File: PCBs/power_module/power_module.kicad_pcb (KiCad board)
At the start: 2 copper layers, 46.2 x 38.5 mm, 30 parts, among them J1 Conn_02x07_Odd_Even, J2 Conn_02x08_Odd_Even, J3 Conn_02x08_Odd_Even, J4 SM07B-GHS-TB, J5 SM03B-GHS-TB, J8 mlx_2pin, J9 SM08B-GHS-TB, U1 SN74LVC1T45DBV

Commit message: 3rd revision: corrected mounting holes
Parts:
- added H1: MountingHole, MountingHole:MountingHole_3.2mm_M3, F.Cu at (125.2, 45.2)
- added H2: MountingHole, MountingHole:MountingHole_3.2mm_M3, F.Cu at (125.2, 80.8)
- added H3: MountingHole, MountingHole:MountingHole_3.2mm_M3, F.Cu at (170.2, 45.2)
- added H4: MountingHole, MountingHole:MountingHole_3.2mm_M3, F.Cu at (170.2, 80.8)
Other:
- board size 46.2 x 38.5 mm -> 49.5 x 40 mm

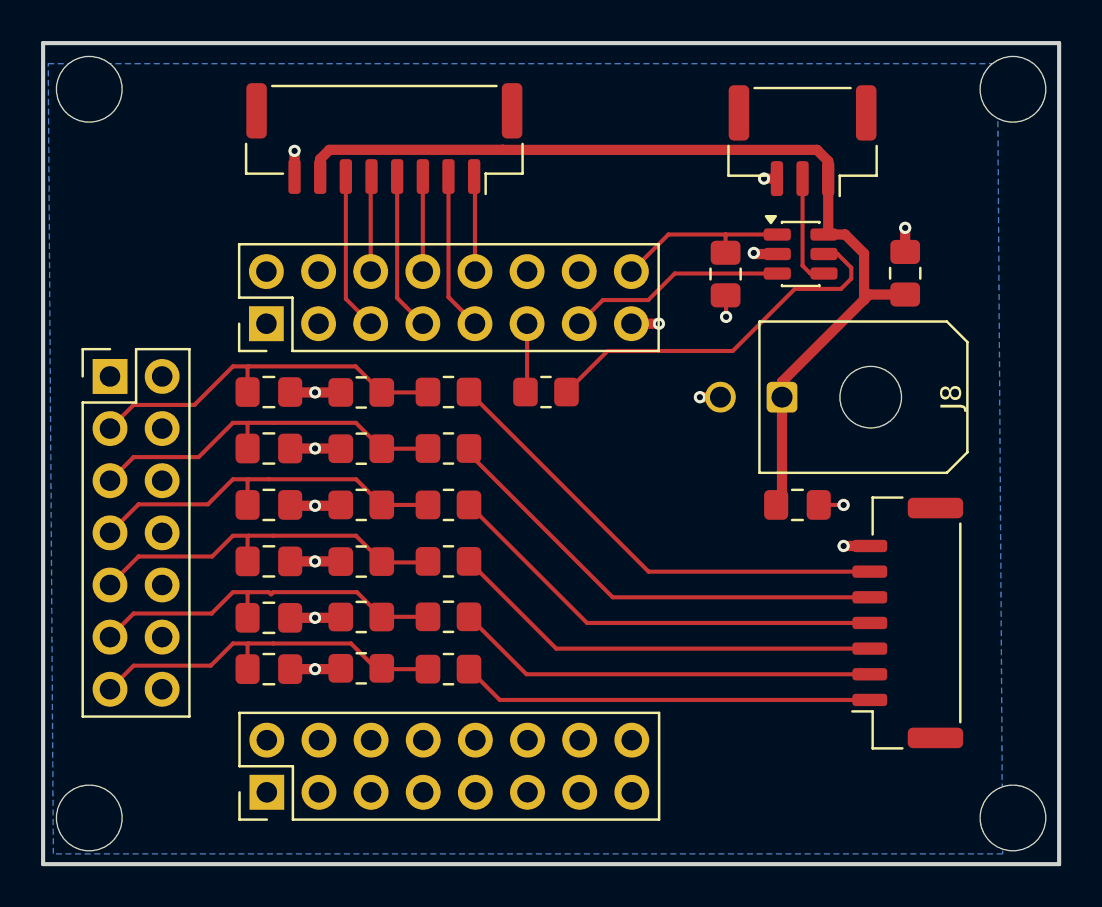
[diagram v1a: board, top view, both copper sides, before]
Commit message: revision 4: shrunk board
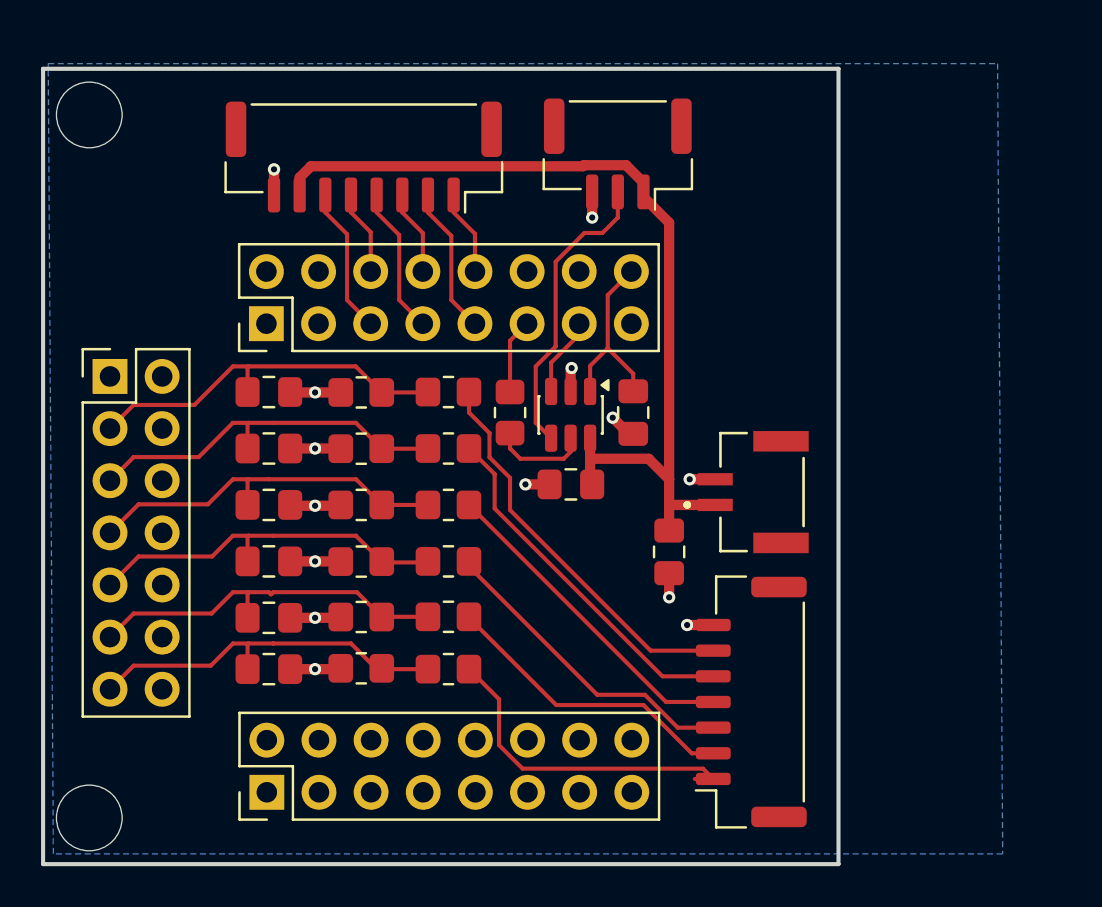
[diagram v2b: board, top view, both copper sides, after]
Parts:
- removed H3, H4: MountingHole, MountingHole:MountingHole_3.2mm_M3
- removed J8: mlx_2pin, Connector_Molex:Molex_Micro-Fit_3.0_43045-0200_2x01_P3.00mm_Horizontal
- added J6: SM02B-GHS-TB, SM02B_GHS:JST_SM02B-GHS-TB, F.Cu at (157.6, 64.9)
- moved C7 17.8 mm to (153.5, 67.8), turned to -90 degrees
- moved U1 13.7 mm to (148.7, 61.1), turned to -90 degrees
- moved C9 11.1 mm to (148.7, 64.5), turned to 180 degrees
- moved J5 9.02 mm to (151.0, 48.4)
- moved J4 8.54 mm to (157.5, 75.1)
- moved C8 8.11 mm to (151.8, 61.0)
- moved R13 2.02 mm to (145.8, 61.0), turned to -90 degrees
- moved J7 1.35 mm to (138.6, 48.5)
- moved H1 1.25 mm to (125.2, 46.5)
- renumbered J9 to J7
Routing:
- net Net-(U1-DIR): track 18.3 -> 4.71 mm
- net Net-(U1-B): track 5.45 -> 14.2 mm
- net /50: track 10.7 -> 3.87 mm
- net Net-(J4-Pad4): track 21.9 -> 15.9 mm
- net Net-(J4-Pad2): track 20.7 -> 14.7 mm
- net Net-(J4-Pad3): track 21.3 -> 15.4 mm
- net +5V: track 49.8 -> 44.2 mm
- net Net-(J4-Pad5): track 22.6 -> 17.7 mm
- net Net-(J4-Pad6): track 23.1 -> 19.3 mm
- net Net-(J4-Pad1): track 20.1 -> 16.3 mm
- net GND: track 24.4 -> 23.9 mm, vias 15 -> 14
- net +3.3V: track 8.74 -> 9.29 mm
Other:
- board size 49.5 x 40 mm -> 38.8 x 38.8 mm

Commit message: revision 5: added mounting holes
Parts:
- added H3: MountingHole, MountingHole:MountingHole_3.2mm_M3, F.Cu at (159.5, 46.5)
- added H4: MountingHole, MountingHole:MountingHole_3.2mm_M3, F.Cu at (159.5, 80.8)
- moved C7 12.7 mm to (158.2, 56.0), turned to 0 degrees
- moved J4 4.61 mm to (157.8, 70.5)
- moved J6 4.36 mm to (158.0, 60.5)
- moved C8 1.02 mm to (152.8, 60.8)
- moved U1 0.85 mm to (149.6, 61.1)
- moved C9 0.75 mm to (149.5, 64.5)
- moved R13 0.75 mm to (146.5, 61.0)
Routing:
- net +5V: track 44.2 -> 48.1 mm
- net Net-(J4-Pad1): track 16.3 -> 12.6 mm
- net Net-(J4-Pad6): track 19.3 -> 16.4 mm
- net Net-(J4-Pad5): track 17.7 -> 15.2 mm
- net Net-(J4-Pad3): track 15.4 -> 13.7 mm
- net Net-(J4-Pad2): track 14.7 -> 13.1 mm
- net Net-(J4-Pad4): track 15.9 -> 14.3 mm

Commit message: cleaned up folders
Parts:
- moved H1 0.25 mm to (125.5, 46.5)
- moved H2 0.25 mm to (125.5, 80.8)
- moved H3 0.25 mm to (159.8, 46.5)
- moved H4 0.25 mm to (159.8, 80.8)
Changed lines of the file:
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@@
 		)
 		(embedded_fonts no)
-		(model "${KIPRJMOD}/SM02B_GHS_TB/SM02B-GHS-TB.step"
+		(model "${KIPRJMOD}/imported_connector_files/SM02B_GHS_TB/SM02B-GHS-TB.step"
 			(offset
 				(xyz 0 -0.3 0)
@@
 	(footprint "MountingHole:MountingHole_3.2mm_M3"
 		(layer "F.Cu")
-		(at 159.5 46.5)
+		(at 159.75 46.5)
 		(descr "Mounting Hole 3.2mm, M3, no annular, generated by kicad-footprint-generator mountinghole.py")
 		(tags "mountinghole M3")
@@
 	(footprint "MountingHole:MountingHole_3.2mm_M3"
 		(layer "F.Cu")
-		(at 125.25 46.5)
+		(at 125.5 46.5)
 		(descr "Mounting Hole 3.2mm, M3, no annular, generated by kicad-footprint-generator mountinghole.py")
 		(tags "mountinghole M3")
@@
 	(footprint "MountingHole:MountingHole_3.2mm_M3"
 		(layer "F.Cu")
-		(at 125.25 80.75)
+		(at 125.5 80.75)
 		(descr "Mounting Hole 3.2mm, M3, no annular, generated by kicad-footprint-generator mountinghole.py")
 		(tags "mountinghole M3")
@@
 	(footprint "MountingHole:MountingHole_3.2mm_M3"
 		(layer "F.Cu")
-		(at 159.5 80.75)
+		(at 159.75 80.75)
 		(descr "Mounting Hole 3.2mm, M3, no annular, generated by kicad-footprint-generator mountinghole.py")
 		(tags "mountinghole M3")
@@
 	)
 	(gr_rect
-		(start 123 44.25)
-		(end 161.75 83)
+		(start 123.25 44.25)
+		(end 162 83)
 		(stroke
 			(width 0.2)
@@
 	)
 	(gr_text "5V In"
-		(at 163.5 66.75 90)
+		(at 163.75 62.25 90)
 		(layer "Cmts.User")
 		(effects
@@
 	)
 	(gr_text "Battery In\n"
-		(at 163.25 78.5 90)
+		(at 163.75 74 90)
 		(layer "Cmts.User")
 		(effects
@@
 	)
 	(gr_text "Relays Out"
-		(at 134.75 43.75 0)
+		(at 134.25 43.75 0)
 		(layer "Cmts.User")
 		(effects
@@
 	)
 	(gr_text "Level Shifter Out"
-		(at 145 43.75 0)
+		(at 144.5 43.75 0)
 		(layer "Cmts.User")
 		(effects
@@
 		(layer "Dwgs.User")
 		(pts
-			(xy 123 44.25) (xy 123 83)
+			(xy 123.25 44.25) (xy 123.25 83)
 		)
 		(height -4.5)
@@
 		)
 		(gr_text "38.7500 mm"
-			(at 117.35 63.625 90)
+			(at 117.6 63.625 90)
 			(layer "Dwgs.User")
 			(effects
@@
 		(layer "Dwgs.User")
 		(pts
-			(xy 123 83) (xy 161.75 83)
+			(xy 123.25 83) (xy 162 83)
 		)
 		(height 6.75)
@@
 		)
 		(gr_text "38.7500 mm"
-			(at 142.375 88.6 0)
+			(at 142.625 88.6 0)
 			(layer "Dwgs.User")
 			(effects
